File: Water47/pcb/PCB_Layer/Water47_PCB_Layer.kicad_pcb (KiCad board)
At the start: 2 copper layers, 260 x 76.5 mm, 107 parts, among them SW1 Esc, SW10 O, SW11 P, SW12 -, SW13 Del, SW14 Cmd, SW15 A, SW16 S, SW17 D, SW18 F, SW19 G, SW2 Q, SW20 H, SW21 J, SW22 K, SW23 L, SW24 ;, SW25 Bs, SW26 Shift(L), SW27 Z, SW28 X, SW29 C, SW3 W, SW30 V, SW31 B, SW32 N, SW33 M, SW34 ,, SW35 ., SW36 Shift(R), SW37 Fn, SW38 Ctrl(L), SW39 Win(L), SW4 E, SW40 Alt(L), SW41 Shift(C), SW42 Fn(C), SW43 Enter, SW44 ←, SW45 ↓, SW46 ↑, SW47 →, SW5 R, SW6 T, SW7 Y, SW8 U, SW9 I, U1 Seeeduino XIAO

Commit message: feat: add symbol, annotating
add MoutingHoles
update annotating
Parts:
- U1: value Seeeduino XIAO -> MOUDLE-SEEEDUINO-XIAO

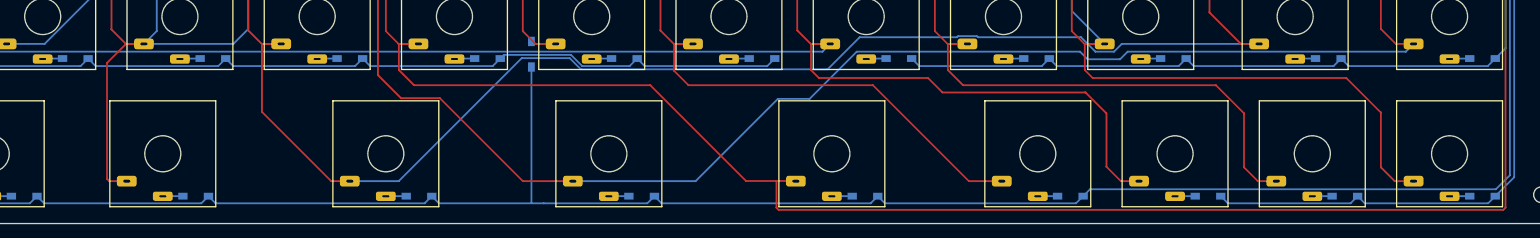
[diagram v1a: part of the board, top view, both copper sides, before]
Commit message: feat: change key layout
2u -> 1.75u to not put stabilizer
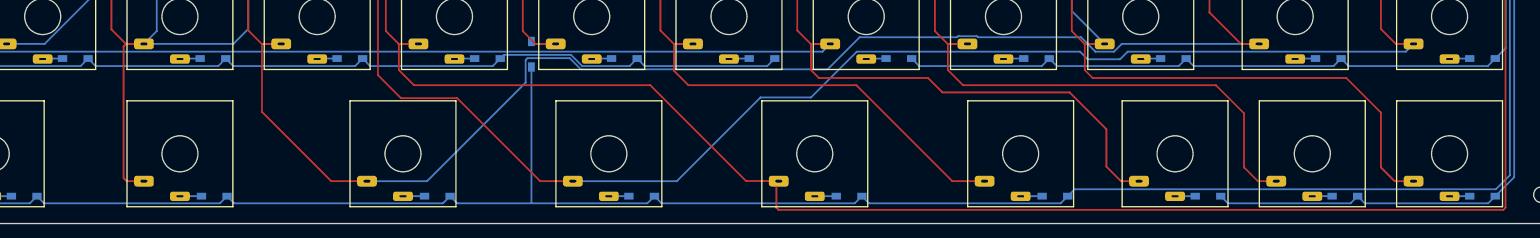
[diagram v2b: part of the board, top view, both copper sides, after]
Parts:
- SW40: footprint multifeb13_kbd_KiCad_lib:Kailh_Choc_V2_1.25u_wo_anker -> multifeb13_kbd_KiCad_lib:Kailh_Choc_V2_1.5u_wo_anker
- SW41, SW43: footprint multifeb13_kbd_KiCad_lib:Kailh_Choc_V2_2u_wo_anker -> multifeb13_kbd_KiCad_lib:Kailh_Choc_V2_1.75u_wo_anker
- SW44: footprint multifeb13_kbd_KiCad_lib:Kailh_Choc_V2_1u_wo_anker -> multifeb13_kbd_KiCad_lib:Kailh_Choc_V2_1.25u_wo_anker
- moved D40 2.58 mm to (154.8, 155.9)
- moved D41 2.54 mm to (185.7, 155.9)
- moved SW40 2.38 mm to (150.0, 150.0)
- moved SW44 2.38 mm to (266.7, 150.0)
- moved SW41 2.38 mm to (181.0, 150.0)
- moved SW43 2.38 mm to (238.1, 150.0)
- moved D43 2.21 mm to (242.9, 155.9)
- moved D44 2.14 mm to (271.5, 155.9)
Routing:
- net Net-(D55-Pad1): track 216.5 -> 214.1 mm
- net Net-(D53-Pad1): track 334.9 -> 332.5 mm
- net Net-(D51-Pad1): track 380.7 -> 382.5 mm
- net Net-(D48-Pad1): track 312.9 -> 311.6 mm
- net Net-(D50-Pad1): track 389.8 -> 388.9 mm

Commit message: feat: change micon direction
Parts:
- moved D13 6.07 mm to (328.4, 87.8), turned to 180 degrees
- moved U1 3.39 mm to (326.2, 95.5), turned to 0 degrees
- turned SW13 to 0 degrees
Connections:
- U1 pad 10: PIN6 -> PIN2
- U1 pad 11: PIN4 -> PIN5
- U1 pad 2: unconnected-(U1-Pad2) -> PIN8
- U1 pad 3: PIN5 -> unconnected-(U1-Pad3)
- U1 pad 4: PIN3 -> PIN7
- U1 pad 7: PIN8 -> PIN6
- U1 pad 8: PIN7 -> PIN4
- U1 pad 9: PIN2 -> PIN3
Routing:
- net PIN3: track 246.8 -> 227.8 mm
- net PIN1: track 229.9 -> 243.3 mm
- net PIN2: track 101.6 -> 89.3 mm
- net Net-(D51-Pad1): track 382.5 -> 372.3 mm
- net PIN8: track 152.8 -> 145.4 mm
- net PIN5: track 415.6 -> 410.0 mm
- net Net-(D13-Pad2): track 8.16 -> 13.6 mm
- net PIN6: track 124.5 -> 120.4 mm
- net PIN7: track 307.0 -> 310.1 mm

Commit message: feat: change mounting spacer to hex
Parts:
- H1, H2, H3, H4: footprint kbd_Hole:m2_Screw_Hole -> kbd_Hole:m2_Spacer_Hole_hex
- turned H1 to 90 degrees
- turned H2 to 90 degrees
- turned H3 to 90 degrees
- turned H4 to 90 degrees
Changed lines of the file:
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@@
     )
   )
-  (footprint "kbd_Hole:m2_Screw_Hole" (layer "F.Cu")
-    (at 85 87.2)
+  (footprint "kbd_Hole:m2_Spacer_Hole_hex" (layer "F.Cu")
+    (at 85 87.2 90)
     (descr "Mounting Hole 2.2mm, no annular, M2")
     (tags "mounting hole 2.2mm no annular m2")
     (property "Sheetfile" "Water47_PCB_Layer.kicad_sch")
     (property "Sheetname" "")
-    (autoplace_cost90 1)
     (attr exclude_from_pos_files)
-    (fp_text reference "H1" (at 0 -3.2) (layer "F.Fab")
-      (effects (font (size 1 1) (thickness 0.15)))
-    )
-    (fp_text value "MountingHole" (at 0 3.2) (layer "F.Fab") hide
-      (effects (font (size 1 1) (thickness 0.15)))
-    )
-    (fp_text user "${REFERENCE}" (at 0.3 0) (layer "F.Fab") hide
-      (effects (font (size 1 1) (thickness 0.15)))
-    )
-    (fp_circle (center 0 0) (end 2.2 0) (layer "Cmts.User") (width 0.15) (fill none))
-    (fp_circle (center 0 0) (end 2.45 0) (layer "F.CrtYd") (width 0.05) (fill none))
-    (pad "" np_thru_hole circle locked (at 0 0) (size 2.2 2.2) (drill 2.2) (layers *.Cu *.Mask))
+    (fp_text reference "H1" (at 0 -3.2 90) (layer "F.Fab")
+      (effects (font (size 1 1) (thickness 0.15)))
+    )
+    (fp_text value "MountingHole" (at 0 3.2 90) (layer "F.Fab")
+      (effects (font (size 1 1) (thickness 0.15)))
+    )
+    (fp_line (start -1.2 2.15) (end 1.2 2.15) (layer "Edge.Cuts") (width 0.1))
+    (fp_line (start 1.2 2.15) (end 2.4 0) (layer "Edge.Cuts") (width 0.1))
+    (fp_line (start 2.4 0) (end 1.2 -2.15) (layer "Edge.Cuts") (width 0.1))
+    (fp_line (start -1.2 -2.15) (end -2.4 0) (layer "Edge.Cuts") (width 0.1))
+    (fp_line (start 1.2 -2.15) (end -1.2 -2.15) (layer "Edge.Cuts") (width 0.1))
+    (fp_line (start -2.4 0) (end -1.2 2.15) (layer "Edge.Cuts") (width 0.1))
   )
   (footprint "multifeb13_kbd_KiCad_lib:Kailh_Choc_V2_1.25u_wo_anker" (layer "F.Cu")
@@
       (net 33 "Net-(D36-Pad2)") (pinfunction "2") (pintype "passive"))
   )
-  (footprint "kbd_Hole:m2_Screw_Hole" (layer "F.Cu")
-    (at 85 155.7)
+  (footprint "kbd_Hole:m2_Spacer_Hole_hex" (layer "F.Cu")
+    (at 85 155.7 90)
     (descr "Mounting Hole 2.2mm, no annular, M2")
     (tags "mounting hole 2.2mm no annular m2")
@@
     (property "Sheetname" "")
     (attr exclude_from_pos_files)
-    (fp_text reference "H2" (at 0 -3.2) (layer "F.Fab")
-      (effects (font (size 1 1) (thickness 0.15)))
-    )
-    (fp_text value "MountingHole" (at 0 3.2) (layer "F.Fab") hide
-      (effects (font (size 1 1) (thickness 0.15)))
-    )
-    (fp_text user "${REFERENCE}" (at 0.3 0) (layer "F.Fab") hide
-      (effects (font (size 1 1) (thickness 0.15)))
-    )
-    (fp_circle (center 0 0) (end 2.2 0) (layer "Cmts.User") (width 0.15) (fill none))
-    (fp_circle (center 0 0) (end 2.45 0) (layer "F.CrtYd") (width 0.05) (fill none))
-    (pad "" np_thru_hole circle locked (at 0 0) (size 2.2 2.2) (drill 2.2) (layers *.Cu *.Mask))
+    (fp_text reference "H2" (at 0 -3.2 90) (layer "F.Fab")
+      (effects (font (size 1 1) (thickness 0.15)))
+    )
+    (fp_text value "MountingHole" (at 0 3.2 90) (layer "F.Fab")
+      (effects (font (size 1 1) (thickness 0.15)))
+    )
+    (fp_line (start 1.2 -2.15) (end -1.2 -2.15) (layer "Edge.Cuts") (width 0.1))
+    (fp_line (start -2.4 0) (end -1.2 2.15) (layer "Edge.Cuts") (width 0.1))
+    (fp_line (start 2.4 0) (end 1.2 -2.15) (layer "Edge.Cuts") (width 0.1))
+    (fp_line (start -1.2 -2.15) (end -2.4 0) (layer "Edge.Cuts") (width 0.1))
+    (fp_line (start -1.2 2.15) (end 1.2 2.15) (layer "Edge.Cuts") (width 0.1))
+    (fp_line (start 1.2 2.15) (end 2.4 0) (layer "Edge.Cuts") (width 0.1))
   )
   (footprint "multifeb13_kbd_KiCad_lib:Kailh_Choc_V2_1u_wo_anker" (layer "F.Cu")
@@
     )
   )
-  (footprint "kbd_Hole:m2_Screw_Hole" (layer "F.Cu")
-    (at 339 155.7)
+  (footprint "kbd_Hole:m2_Spacer_Hole_hex" (layer "F.Cu")
+    (at 339 155.7 90)
     (descr "Mounting Hole 2.2mm, no annular, M2")
     (tags "mounting hole 2.2mm no annular m2")
@@
     (property "Sheetname" "")
     (attr exclude_from_pos_files)
-    (fp_text reference "H4" (at 0 -3.2) (layer "F.Fab") hide
-      (effects (font (size 1 1) (thickness 0.15)))
-    )
-    (fp_text value "MountingHole" (at 0 3.2) (layer "F.Fab") hide
-      (effects (font (size 1 1) (thickness 0.15)))
-    )
-    (fp_text user "${REFERENCE}" (at 0.3 0) (layer "F.Fab") hide
-      (effects (font (size 1 1) (thickness 0.15)))
-    )
-    (fp_circle (center 0 0) (end 2.2 0) (layer "Cmts.User") (width 0.15) (fill none))
-    (fp_circle (center 0 0) (end 2.45 0) (layer "F.CrtYd") (width 0.05) (fill none))
-    (pad "" np_thru_hole circle locked (at 0 0) (size 2.2 2.2) (drill 2.2) (layers *.Cu *.Mask))
+    (fp_text reference "H4" (at 0 -3.2 90) (layer "F.Fab")
+      (effects (font (size 1 1) (thickness 0.15)))
+    )
+    (fp_text value "MountingHole" (at 0 3.2 90) (layer "F.Fab")
+      (effects (font (size 1 1) (thickness 0.15)))
+    )
+    (fp_line (start 2.4 0) (end 1.2 -2.15) (layer "Edge.Cuts") (width 0.1))
+    (fp_line (start 1.2 -2.15) (end -1.2 -2.15) (layer "Edge.Cuts") (width 0.1))
+    (fp_line (start -1.2 -2.15) (end -2.4 0) (layer "Edge.Cuts") (width 0.1))
+    (fp_line (start -2.4 0) (end -1.2 2.15) (layer "Edge.Cuts") (width 0.1))
+    (fp_line (start 1.2 2.15) (end 2.4 0) (layer "Edge.Cuts") (width 0.1))
+    (fp_line (start -1.2 2.15) (end 1.2 2.15) (layer "Edge.Cuts") (width 0.1))
   )
   (footprint "kbd_Parts:Diode_SMD" (layer "F.Cu")
@@
       (net 29 "Net-(D30-Pad2)") (pinfunction "2") (pintype "passive"))
   )
-  (footprint "kbd_Hole:m2_Screw_Hole" (layer "F.Cu")
-    (at 339 87.2)
+  (footprint "kbd_Hole:m2_Spacer_Hole_hex" (layer "F.Cu")
+    (at 339 87.2 90)
     (descr "Mounting Hole 2.2mm, no annular, M2")
     (tags "mounting hole 2.2mm no annular m2")
@@
     (property "Sheetname" "")
     (attr exclude_from_pos_files)
-    (fp_text reference "H3" (at 0 -3.2) (layer "F.Fab")
-      (effects (font (size 1 1) (thickness 0.15)))
-    )
-    (fp_text value "MountingHole" (at 0 3.2) (layer "F.Fab")
-      (effects (font (size 1 1) (thickness 0.15)))
-    )
-    (fp_text user "${REFERENCE}" (at 0.3 0) (layer "F.Fab") hide
-      (effects (font (size 1 1) (thickness 0.15)))
-    )
-    (fp_circle (center 0 0) (end 2.2 0) (layer "Cmts.User") (width 0.15) (fill none))
-    (fp_circle (center 0 0) (end 2.45 0) (layer "F.CrtYd") (width 0.05) (fill none))
-    (pad "" np_thru_hole circle locked (at 0 0) (size 2.2 2.2) (drill 2.2) (layers *.Cu *.Mask))
-  )
-  (footprint "kbd_Parts:Diode_SMD" (layer "F.Cu")
+    (fp_text reference "H3" (at 0 -3.2 90) (layer "F.Fab")
+      (effects (font (size 1 1) (thickness 0.15)))
+    )
+    (fp_text value "MountingHole" (at 0 3.2 90) (layer "F.Fab")
+      (effects (font (size 1 1) (thickness 0.15)))
+    )
+    (fp_line (start -2.4 0) (end -1.2 2.15) (layer "Edge.Cuts") (width 0.1))
+    (fp_line (start 1.2 -2.15) (end -1.2 -2.15) (layer "Edge.Cuts") (width 0.1))
+    (fp_line (start -1.2 2.15) (end 1.2 2.15) (layer "Edge.Cuts") (width 0.1))
+    (fp_line (start -1.2 -2.15) (end -2.4 0) (layer "Edge.Cuts") (width 0.1))
+    (fp_line (start 1.2 2.15) (end 2.4 0) (layer "Edge.Cuts") (width 0.1))
+    (fp_line (start 2.4 0) (end 1.2 -2.15) (layer "Edge.Cuts") (width 0.1))
+  )
+  (footprint "kbd_Parts:Diode_SMD" (layer "F.Cu")

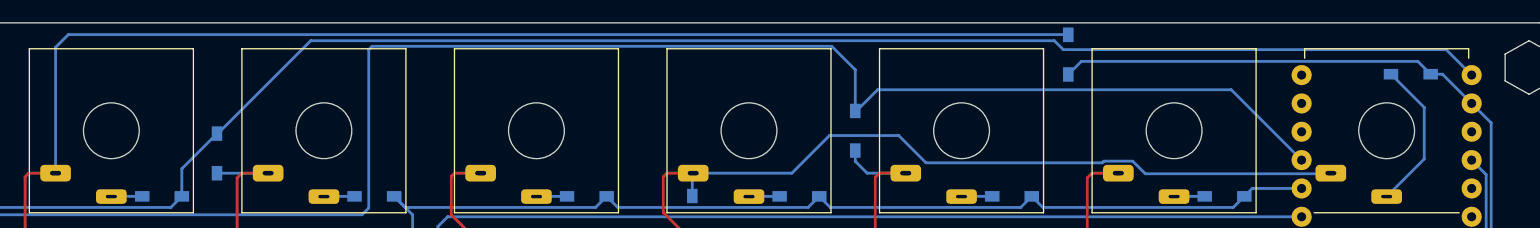
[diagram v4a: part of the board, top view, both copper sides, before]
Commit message: fix: clearance between diode and PCB edge
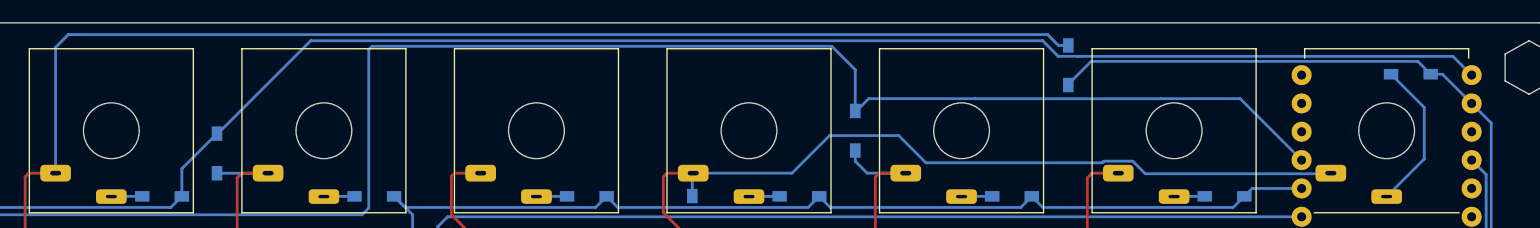
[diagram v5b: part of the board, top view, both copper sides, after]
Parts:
- moved D55 0.95 mm to (297.7, 87.0)
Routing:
- net PIN5: track 410.0 -> 409.3 mm
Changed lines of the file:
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@@
       (drillshape 0)
       (scaleselection 1)
-      (outputdirectory "../../gerber/PCB_Layer1/")
+      (outputdirectory "../../gerber/PCB_Layer/")
     )
   )
@@
   )
   (footprint "kbd_Parts:Diode_SMD" (layer "F.Cu")
-    (at 297.7 86.05 -90)
+    (at 297.7 87 -90)
     (descr "Resitance 3 pas")
     (tags "R")
@@
     (style (thickness 0.2) (arrow_length 1.27) (text_position_mode 0) (extension_height 0.58642) (extension_offset 0.5) keep_text_aligned)
   )
-  (segment (start 296.45 84.8) (end 297.25 85.6) (width 0.25) (layer "B.Cu") (net 1))
+  (segment (start 229.8 84.8) (end 295.4 84.8) (width 0.25) (layer "B.Cu") (net 1))
   (segment (start 141.03125 99.74375) (end 123.96875 99.74375) (width 0.25) (layer "B.Cu") (net 1))
   (segment (start 218.25 98.75) (end 217.25625 99.74375) (width 0.25) (layer "B.Cu") (net 1))
   (segment (start 180.125 98.75) (end 179.13125 99.74375) (width 0.25) (layer "B.Cu") (net 1))
   (segment (start 181.11875 99.74375) (end 180.125 98.75) (width 0.25) (layer "B.Cu") (net 1))
+  (segment (start 221.475 93.125) (end 229.8 84.8) (width 0.25) (layer "B.Cu") (net 1))
   (segment (start 179.13125 99.74375) (end 162.06875 99.74375) (width 0.25) (layer "B.Cu") (net 1))
   (segment (start 122.975 98.75) (end 121.98125 99.74375) (width 0.25) (layer "B.Cu") (net 1))
-  (segment (start 229.8 84.8) (end 296.45 84.8) (width 0.25) (layer "B.Cu") (net 1))
+  (segment (start 298.5 86.2) (end 298.505 86.205) (width 0.25) (layer "B.Cu") (net 1))
   (segment (start 160.08125 99.74375) (end 143.01875 99.74375) (width 0.25) (layer "B.Cu") (net 1))
   (segment (start 123.96875 99.74375) (end 122.975 98.75) (width 0.25) (layer "B.Cu") (net 1))
   (segment (start 104.9625 99.74375) (end 103.96875 98.75) (width 0.25) (layer "B.Cu") (net 1))
   (segment (start 143.01875 99.74375) (end 142.025 98.75) (width 0.25) (layer "B.Cu") (net 1))
+  (segment (start 298.505 86.205) (end 332.17625 86.205) (width 0.25) (layer "B.Cu") (net 1))
   (segment (start 142.025 98.75) (end 141.03125 99.74375) (width 0.25) (layer "B.Cu") (net 1))
-  (segment (start 221.4 93.125) (end 221.475 93.125) (width 0.25) (layer "B.Cu") (net 1))
+  (segment (start 296.8 86.2) (end 298.5 86.2) (width 0.25) (layer "B.Cu") (net 1))
   (segment (start 217.25625 99.74375) (end 200.21875 99.74375) (width 0.25) (layer "B.Cu") (net 1))
   (segment (start 161.075 98.75) (end 160.08125 99.74375) (width 0.25) (layer "B.Cu") (net 1))
@@
   (segment (start 199.225 98.75) (end 198.23125 99.74375) (width 0.25) (layer "B.Cu") (net 1))
   (segment (start 162.06875 99.74375) (end 161.075 98.75) (width 0.25) (layer "B.Cu") (net 1))
-  (segment (start 331.57125 85.6) (end 333.85125 87.88) (width 0.25) (layer "B.Cu") (net 1))
-  (segment (start 297.25 85.6) (end 331.57125 85.6) (width 0.25) (layer "B.Cu") (net 1))
+  (segment (start 221.4 93.125) (end 221.475 93.125) (width 0.25) (layer "B.Cu") (net 1))
+  (segment (start 332.17625 86.205) (end 333.85125 87.88) (width 0.25) (layer "B.Cu") (net 1))
   (segment (start 218.25 96.275) (end 218.25 98.75) (width 0.25) (layer "B.Cu") (net 1))
-  (segment (start 221.475 93.125) (end 229.8 84.8) (width 0.25) (layer "B.Cu") (net 1))
   (segment (start 221.4 93.125) (end 218.25 96.275) (width 0.25) (layer "B.Cu") (net 1))
+  (segment (start 295.4 84.8) (end 296.8 86.2) (width 0.25) (layer "B.Cu") (net 1))
   (segment (start 119.425 98.75) (end 116.7 98.75) (width 0.25) (layer "B.Cu") (net 2))
   (segment (start 116.7 98.75) (end 116.68125 98.76875) (width 0.25) (layer "B.Cu") (net 2))
@@
   (segment (start 101.3 119.4) (end 103.2 119.4) (width 0.25) (layer "B.Cu") (net 30))
   (segment (start 110.03125 137.84375) (end 100.485051 137.84375) (width 0.25) (layer "B.Cu") (net 30))
+  (segment (start 278.60625 91.09375) (end 278.70625 91.09375) (width 0.25) (layer "B.Cu") (net 30))
+  (segment (start 289.328366 90) (end 305.984134 90) (width 0.25) (layer "B.Cu") (net 30))
   (segment (start 100.485051 137.84375) (end 97.1 134.458699) (width 0.25) (layer "B.Cu") (net 30))
   (segment (start 155.33125 137.84375) (end 156.375 136.8) (width 0.25) (layer "B.Cu") (net 30))
+  (segment (start 305.984134 90) (end 305.990385 89.993749) (width 0.25) (layer "B.Cu") (net 30))
   (segment (start 194.98125 136.29375) (end 204.299511 136.29375) (width 0.25) (layer "B.Cu") (net 30))
+  (segment (start 279.806251 89.993749) (end 289.322115 89.993749) (width 0.25) (layer "B.Cu") (net 30))
   (segment (start 212.43125 137.84375) (end 213.475 136.8) (width 0.25) (layer "B.Cu") (net 30))
   (segment (start 136.23125 137.84375) (end 137.275 136.8) (width 0.25) (layer "B.Cu") (net 30))
+  (segment (start 313.104999 89.993749) (end 318.61125 95.5) (width 0.25) (layer "B.Cu") (net 30))
   (segment (start 175.375 136.8) (end 176.41875 137.84375) (width 0.25) (layer "B.Cu") (net 30))
   (segment (start 104.6 113.6) (end 117.8 100.4) (width 0.25) (layer "B.Cu") (net 30))
   (segment (start 174.33125 137.84375) (end 175.375 136.8) (width 0.25) (layer "B.Cu") (net 30))
-  (segment (start 312.30625 89.195) (end 318.61125 95.5) (width 0.25) (layer "B.Cu") (net 30))
   (segment (start 97.1 123.6) (end 101.3 119.4) (width 0.25) (layer "B.Cu") (net 30))
   (segment (start 235 99.8) (end 235 85.6) (width 0.25) (layer "B.Cu") (net 30))
@@
   (segment (start 138.31875 137.84375) (end 155.33125 137.84375) (width 0.25) (layer "B.Cu") (net 30))
   (segment (start 104.6 118) (end 104.6 113.6) (width 0.25) (layer "B.Cu") (net 30))
-  (segment (start 280.605 89.195) (end 312.30625 89.195) (width 0.25) (layer "B.Cu") (net 30))
   (segment (start 117.8 100.4) (end 234.4 100.4) (width 0.25) (layer "B.Cu") (net 30))
-  (segment (start 278.70625 91.09375) (end 280.605 89.195) (width 0.25) (layer "B.Cu") (net 30))
   (segment (start 213.475 136.8) (end 214.51875 137.84375) (width 0.25) (layer "B.Cu") (net 30))
   (segment (start 205.849511 137.84375) (end 212.43125 137.84375) (width 0.25) (layer "B.Cu") (net 30))
@@
   (segment (start 112.11875 137.84375) (end 136.23125 137.84375) (width 0.25) (layer "B.Cu") (net 30))
   (segment (start 97.1 134.458699) (end 97.1 123.6) (width 0.25) (layer "B.Cu") (net 30))
-  (segment (start 278.60625 91.09375) (end 278.70625 91.09375) (width 0.25) (layer "B.Cu") (net 30))
+  (segment (start 278.70625 91.09375) (end 279.806251 89.993749) (width 0.25) (layer "B.Cu") (net 30))
+  (segment (start 289.322115 89.993749) (end 289.328366 90) (width 0.25) (layer "B.Cu") (net 30))
   (segment (start 204.299511 136.29375) (end 205.849511 137.84375) (width 0.25) (layer "B.Cu") (net 30))
   (segment (start 194.475 136.8) (end 194.98125 136.29375) (width 0.25) (layer "B.Cu") (net 30))
   (segment (start 157.41875 137.84375) (end 174.33125 137.84375) (width 0.25) (layer "B.Cu") (net 30))
   (segment (start 231.53125 137.84375) (end 232.575 136.8) (width 0.25) (layer "B.Cu") (net 30))
+  (segment (start 305.990385 89.993749) (end 313.104999 89.993749) (width 0.25) (layer "B.Cu") (net 30))
   (segment (start 235.3 85.3) (end 276.5 85.3) (width 0.25) (layer "B.Cu") (net 30))
   (segment (start 235 85.6) (end 235.3 85.3) (width 0.25) (layer "B.Cu") (net 30))
@@
   (segment (start 313.475 155.9) (end 312.48125 156.89375) (width 0.25) (layer "B.Cu") (net 46))
   (segment (start 331.23125 87.8) (end 333.85125 90.42) (width 0.25) (layer "B.Cu") (net 46))
+  (segment (start 330.175 87.8) (end 329.03 86.655) (width 0.25) (layer "B.Cu") (net 46))
+  (segment (start 329.03 86.655) (end 299.745 86.655) (width 0.25) (layer "B.Cu") (net 46))
   (segment (start 335.6 92.16875) (end 333.85125 90.42) (width 0.25) (layer "B.Cu") (net 46))
   (segment (start 332.575 155.9) (end 335.6 152.875) (width 0.25) (layer "B.Cu") (net 46))
-  (segment (start 329.03 86.655) (end 298.87 86.655) (width 0.25) (layer "B.Cu") (net 46))
+  (segment (start 299.745 86.655) (end 297.7 88.7) (width 0.25) (layer "B.Cu") (net 46))
   (segment (start 312.48125 156.89375) (end 295.46875 156.89375) (width 0.25) (layer "B.Cu") (net 46))
-  (segment (start 298.87 86.655) (end 297.7 87.825) (width 0.25) (layer "B.Cu") (net 46))
   (segment (start 314.46875 156.89375) (end 313.475 155.9) (width 0.25) (layer "B.Cu") (net 46))
-  (segment (start 330.175 87.8) (end 329.03 86.655) (width 0.25) (layer "B.Cu") (net 46))
+  (segment (start 297.7 88.7) (end 297.7 88.775) (width 0.25) (layer "B.Cu") (net 46))
   (segment (start 332.575 155.9) (end 331.58125 156.89375) (width 0.25) (layer "B.Cu") (net 46))
   (segment (start 330.175 87.8) (end 331.23125 87.8) (width 0.25) (layer "B.Cu") (net 46))
@@
   (segment (start 218.56875 134.76875) (end 221.21875 134.76875) (width 0.25) (layer "F.Cu") (net 68))
   (segment (start 218.6 134.76875) (end 218.6 138.5) (width 0.25) (layer "F.Cu") (net 68))
-  (segment (start 208.075 84.25) (end 206.93125 85.39375) (width 0.25) (layer "B.Cu") (net 68))
+  (segment (start 296.825 85.225) (end 295.85 84.25) (width 0.25) (layer "B.Cu") (net 68))
   (segment (start 206.93125 85.39375) (end 206.93125 96.66875) (width 0.25) (layer "B.Cu") (net 68))
-  (segment (start 297.7 84.275) (end 297.675 84.25) (width 0.25) (layer "B.Cu") (net 68))
-  (segment (start 297.675 84.25) (end 208.075 84.25) (width 0.25) (layer "B.Cu") (net 68))
+  (segment (start 208.075 84.25) (end 206.93125 85.39375) (width 0.25) (layer "B.Cu") (net 68))
+  (segment (start 297.7 85.225) (end 296.825 85.225) (width 0.25) (layer "B.Cu") (net 68))
+  (segment (start 295.85 84.25) (end 208.075 84.25) (width 0.25) (layer "B.Cu") (net 68))
 )
